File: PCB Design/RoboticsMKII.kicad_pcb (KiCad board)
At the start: 4 copper layers, 89 parts, among them CON1 USB, CON2 BARREL_JACK, P1 Power Sel, P10 Camera, P11 DAC, P12 Reed, P13 SPI, P14 ICSP, P15 Gnd, P16 UART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

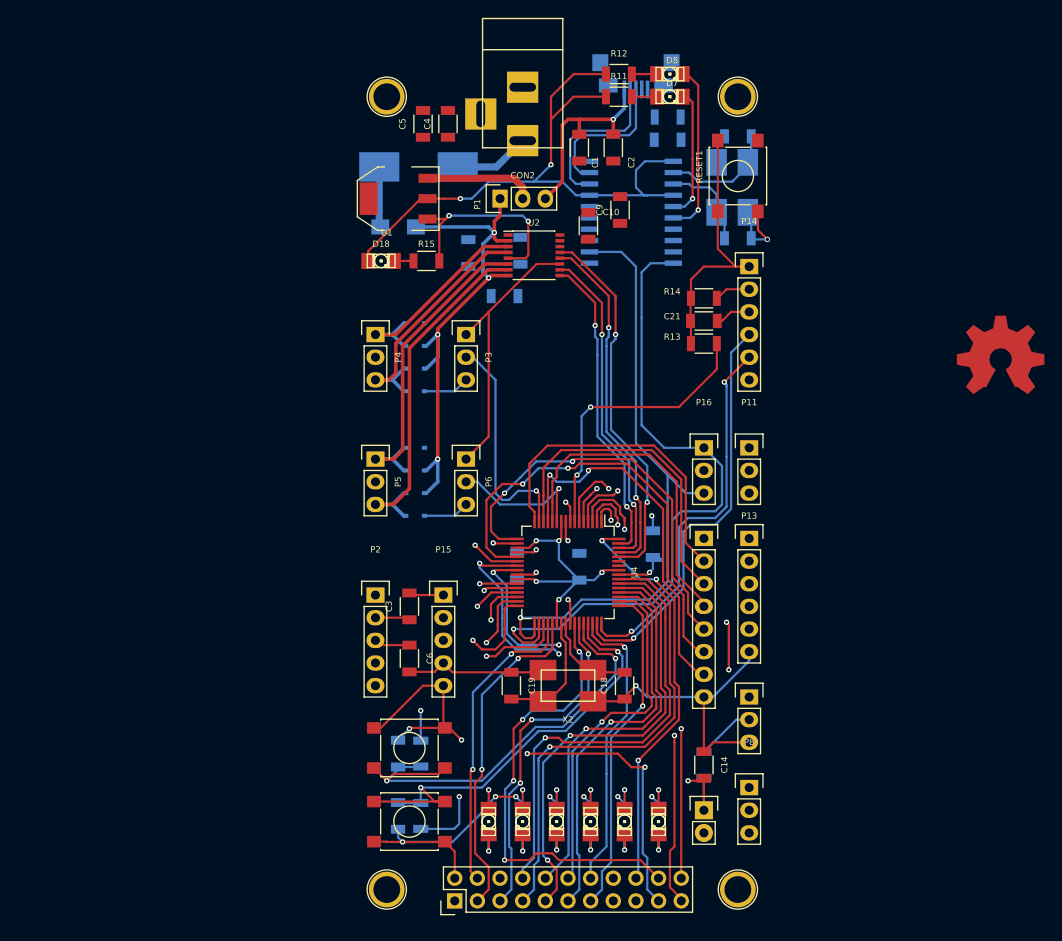
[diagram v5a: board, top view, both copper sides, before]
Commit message: Done with the power layout.
Signed-off-by: Kolijn Wolfaardt <kolijn.wolfaardt@gmail.com>
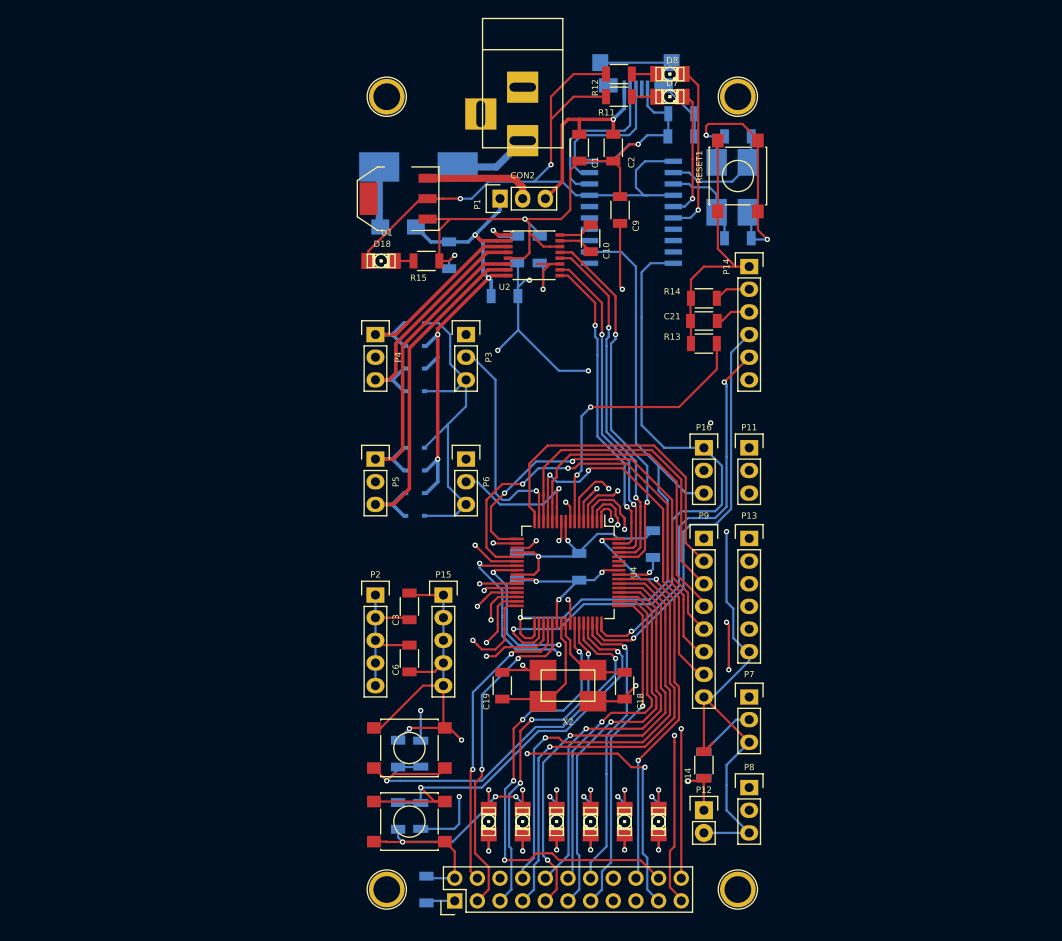
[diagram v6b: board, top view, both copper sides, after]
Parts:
- removed OSHW_COPPER_10MM: VAL**, RoBoC:OSHW_COPPER_10MM
- C4, C5: moved to B.Cu
- moved C5 85.9 mm to (121.3, 135.9)
- moved C4 17.5 mm to (134.0, 64.1)
- moved C23 8.02 mm to (123.8, 64.8)
- moved C11 5.47 mm to (131.4, 64.1)
- moved C17 1.57 mm to (149.9, 51.4), turned to 180 degrees
- moved R10 1.57 mm to (149.9, 48.9), turned to 180 degrees
- moved C10 1.42 mm to (139.7, 62.9)
- moved C19 1.02 mm to (129.8, 113.0)
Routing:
- net GND: track 195.7 -> 569.9 mm, vias 18 -> 24
- net V3.3: track 329.7 -> 474.7 mm, vias 9 -> 11
- net Net-(C17-Pad1): track 0.00 -> 21.2 mm
- net /motors/VG: track 0.00 -> 4.83 mm, vias 0 -> 1
- net /motors/C1L: track 0.00 -> 3.96 mm
- net /motors/C1H: track 0.00 -> 3.92 mm
- net /gpio/DACOUT: track 39.7 -> 42.4 mm
- net /motors/V_Bat: track 60.2 -> 62.6 mm
- net /usb/MCU_TX: track 70.8 -> 72.3 mm
- net /mcu/OSC2: track 14.0 -> 15.4 mm

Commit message: Added an additional cap for the MCU, added copper fill on all layers.
Signed-off-by: Kolijn Wolfaardt <kolijn.wolfaardt@gmail.com>
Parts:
- added C24: 100nF, Capacitors_SMD:C_1206, B.Cu at (140.7, 103.4)
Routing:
- net GND: track 569.9 -> 582.5 mm, vias 24 -> 25
- net V3.3: track 474.7 -> 478.3 mm
- added copper zone on B.Cu, net GND
- added copper zone on F.Cu, net GND
- added copper zone on In1.Cu, net GND
- added copper zone on In2.Cu, net GND

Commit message: Added OSHW logo on the back and front text. Filled copper and generated gerbers.
Signed-off-by: Kolijn Wolfaardt <kolijn.wolfaardt@gmail.com>
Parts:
- added G***: LOGO, OSHW:OSHW_SILK_8mm, B.Cu at (137.2, 76.2)
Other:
- board text added: "Robotics Controller Board"
- board text added: "github.com/KolijnWolfaardt/RoBoC"
